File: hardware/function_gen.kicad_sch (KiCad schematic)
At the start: 19 parts, among them J11 Conn_01x08, SW1 SW_SPDT, SW9 SW_Push, U1 STM32G431CBTx

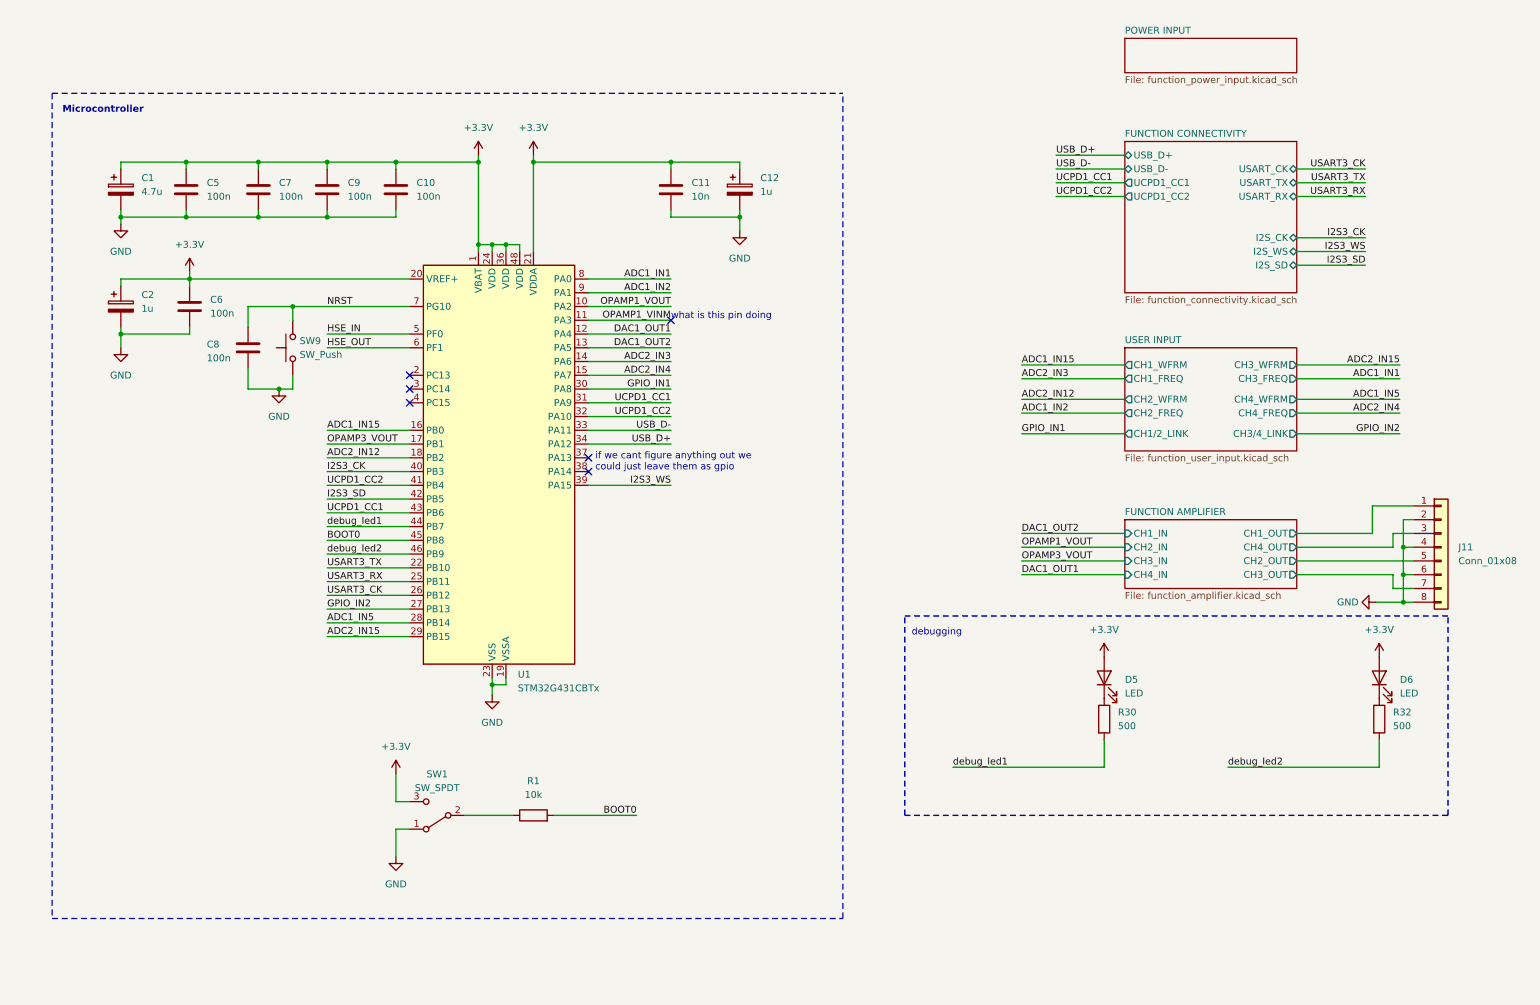
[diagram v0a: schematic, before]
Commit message: added swd header (optional swo), added an led for NRST, added DNP oscillator encase user perfer to use one, added 3 GPIOs
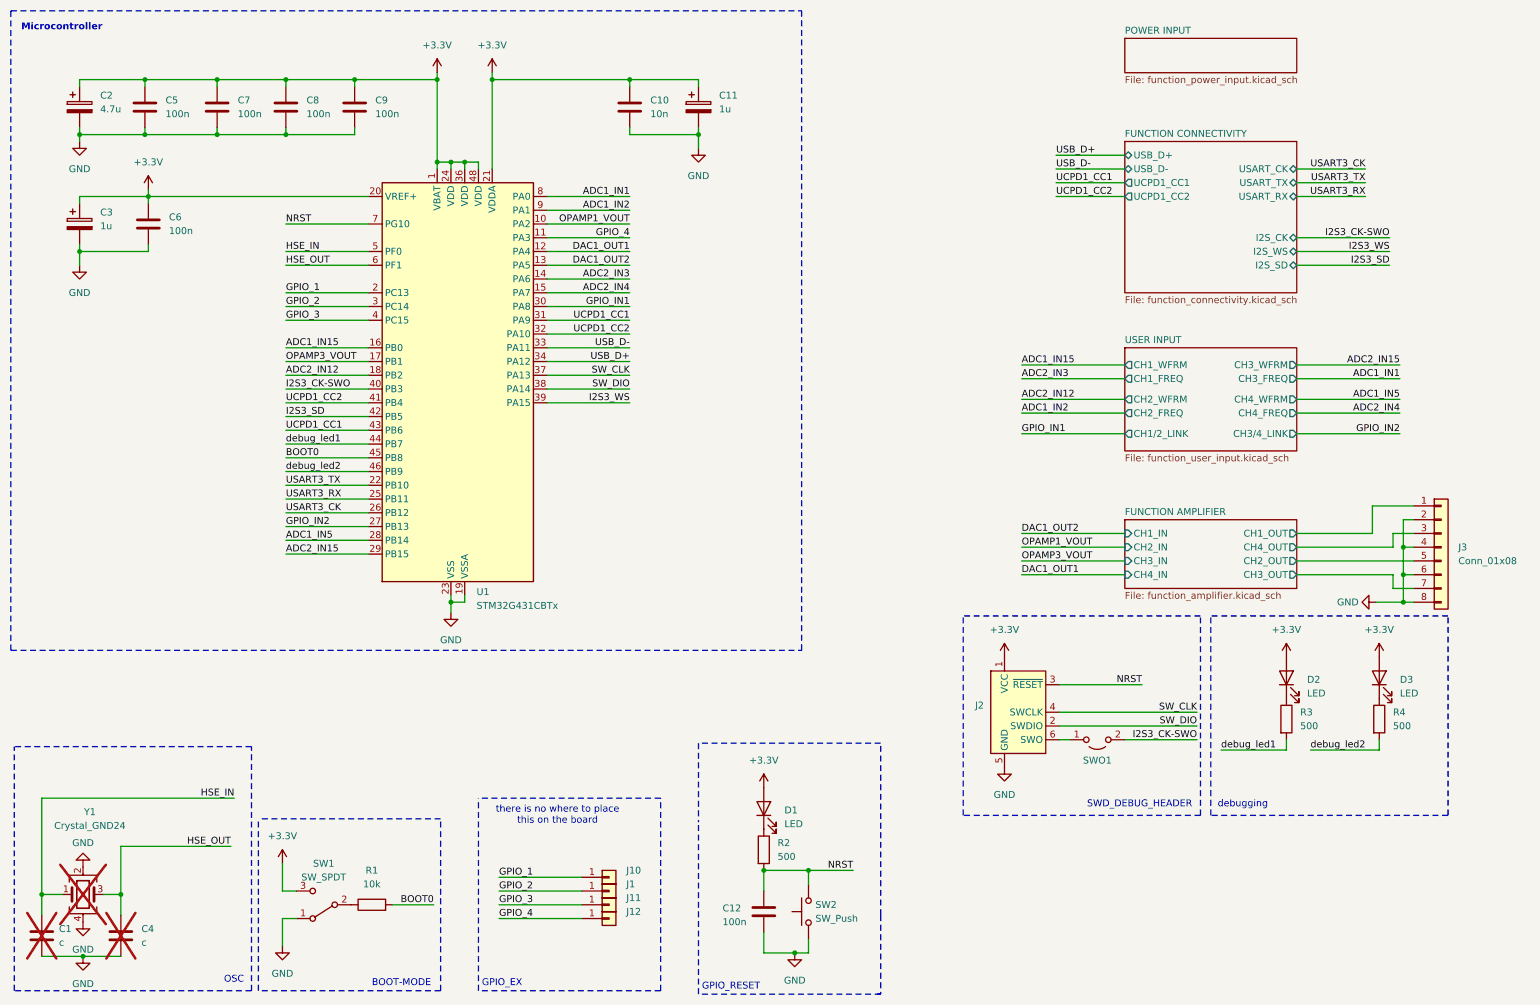
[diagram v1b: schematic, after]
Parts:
- removed C8: 100n, Capacitor_SMD:C_0805_2012Metric, symbol Device:C
- removed SW9: SW_Push, Button_Switch_SMD:SW_Push_SPST_NO_Alps_SKRK, symbol Switch:SW_Push
- added C1, C4: c, Capacitor_SMD:C_0805_2012Metric, symbol Device:C
- added C12: 100n, Capacitor_SMD:C_0805_2012Metric, symbol Device:C
- added D1: LED, LED_SMD:LED_0805_2012Metric, symbol Device:LED
- added J1, J10, J11, J12: Conn_01x01, TestPoint:TestPoint_Pad_1.0x1.0mm, symbol Connector_Generic:Conn_01x01
- added J2: Conn_ARM_SWD_TagConnect_TC2030-NL, Connector:Tag-Connect_TC2030-IDC-NL_2x03_P1.27mm_Vertical, symbol Connector:Conn_ARM_SWD_TagConnect_TC2030-NL
- added R2: 500, Resistor_SMD:R_0805_2012Metric, symbol Device:R
- added SW2: SW_Push, Button_Switch_SMD:SW_Push_SPST_NO_Alps_SKRK, symbol Switch:SW_Push
- added SWO1: Jumper_2_Open, Jumper:SolderJumper-2_P1.3mm_Open_Pad1.0x1.5mm, symbol Jumper:Jumper_2_Open
- added Y1: Crystal_GND24, Crystal:Crystal_SMD_SeikoEpson_FA238V-4Pin_3.2x2.5mm_HandSoldering, symbol Device:Crystal_GND24
- renumbered C11 to C10, C12 to C11, C1 to C2, C2 to C3, C9 to C8, C10 to C9, D5 to D2, D6 to D3, J11 to J3, R30 to R3, R32 to R4
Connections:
- net +3.3V: now also D1.2 (A), J2.1 (VCC)
- net GND: now also C1.2, C12.1, C4.2, J2.5 (GND), SW2.1, Y1.2, Y1.4
- net HSE_IN: now also C1.1, Y1.1
- net HSE_OUT: now also C4.1, Y1.3
- net NRST: now also C12.2, J2.3 (~{RESET}), R2.2, SW2.2
- net GPIO_1: now reaches U1.2 (PC13)
- net GPIO_1: now also J10.1 (Pin_1)
- net GPIO_2: now reaches U1.3 (PC14)
- net GPIO_2: now also J1.1 (Pin_1)
- net SW_CLK: now reaches U1.37 (PA13)
- net SW_CLK: now also J2.4 (SWCLK)
- net SW_DIO: now reaches U1.38 (PA14)
- net SW_DIO: now also J2.2 (SWDIO)
- net GPIO_3: now reaches U1.4 (PC15)
- net GPIO_3: now also J11.1 (Pin_1)
- net I2S3_CK renamed I2S3_CK-SWO
- net I2S3_CK-SWO: now also SWO1.2 (B)
- net OPAMP1_VINM renamed GPIO_4
- net GPIO_4: now also J12.1 (Pin_1)
- new net: J2.6 (SWO), SWO1.1 (A)
- new net: D1.1 (K), R2.1
- no-connect marks 6 -> 0
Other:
- note added: "BOOT-MODE"
- note added: "GPIO_EX"
- note added: "GPIO_RESET"
- note added: "OSC"
- note added: "SWD_DEBUG_HEADER"
- note added: "there is no where to place this on the board"
- note removed: "if we cant figure anything out we could just leave them as gpio"
- note removed: "what is this pin doing"
- moved on the sheet: C10, C11, C2, C3, C5, C6, C7, C8, C9, D2, R1, R3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
